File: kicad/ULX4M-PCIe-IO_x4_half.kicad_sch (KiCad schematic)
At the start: 13 parts, among them J10 FCR684205R, J3 SFP+, J4 SFP+, J5 Conn_02x20_Odd_Even, J6 Conn_02x05_Odd_Even, J7 Micro_SD_Card_CD, J8 Conn_02x05_Odd_Even, J9 FCR684205T, P1 HDMI-D, SW1 SW_DIP_x08, SW2 SW_DIP_x08

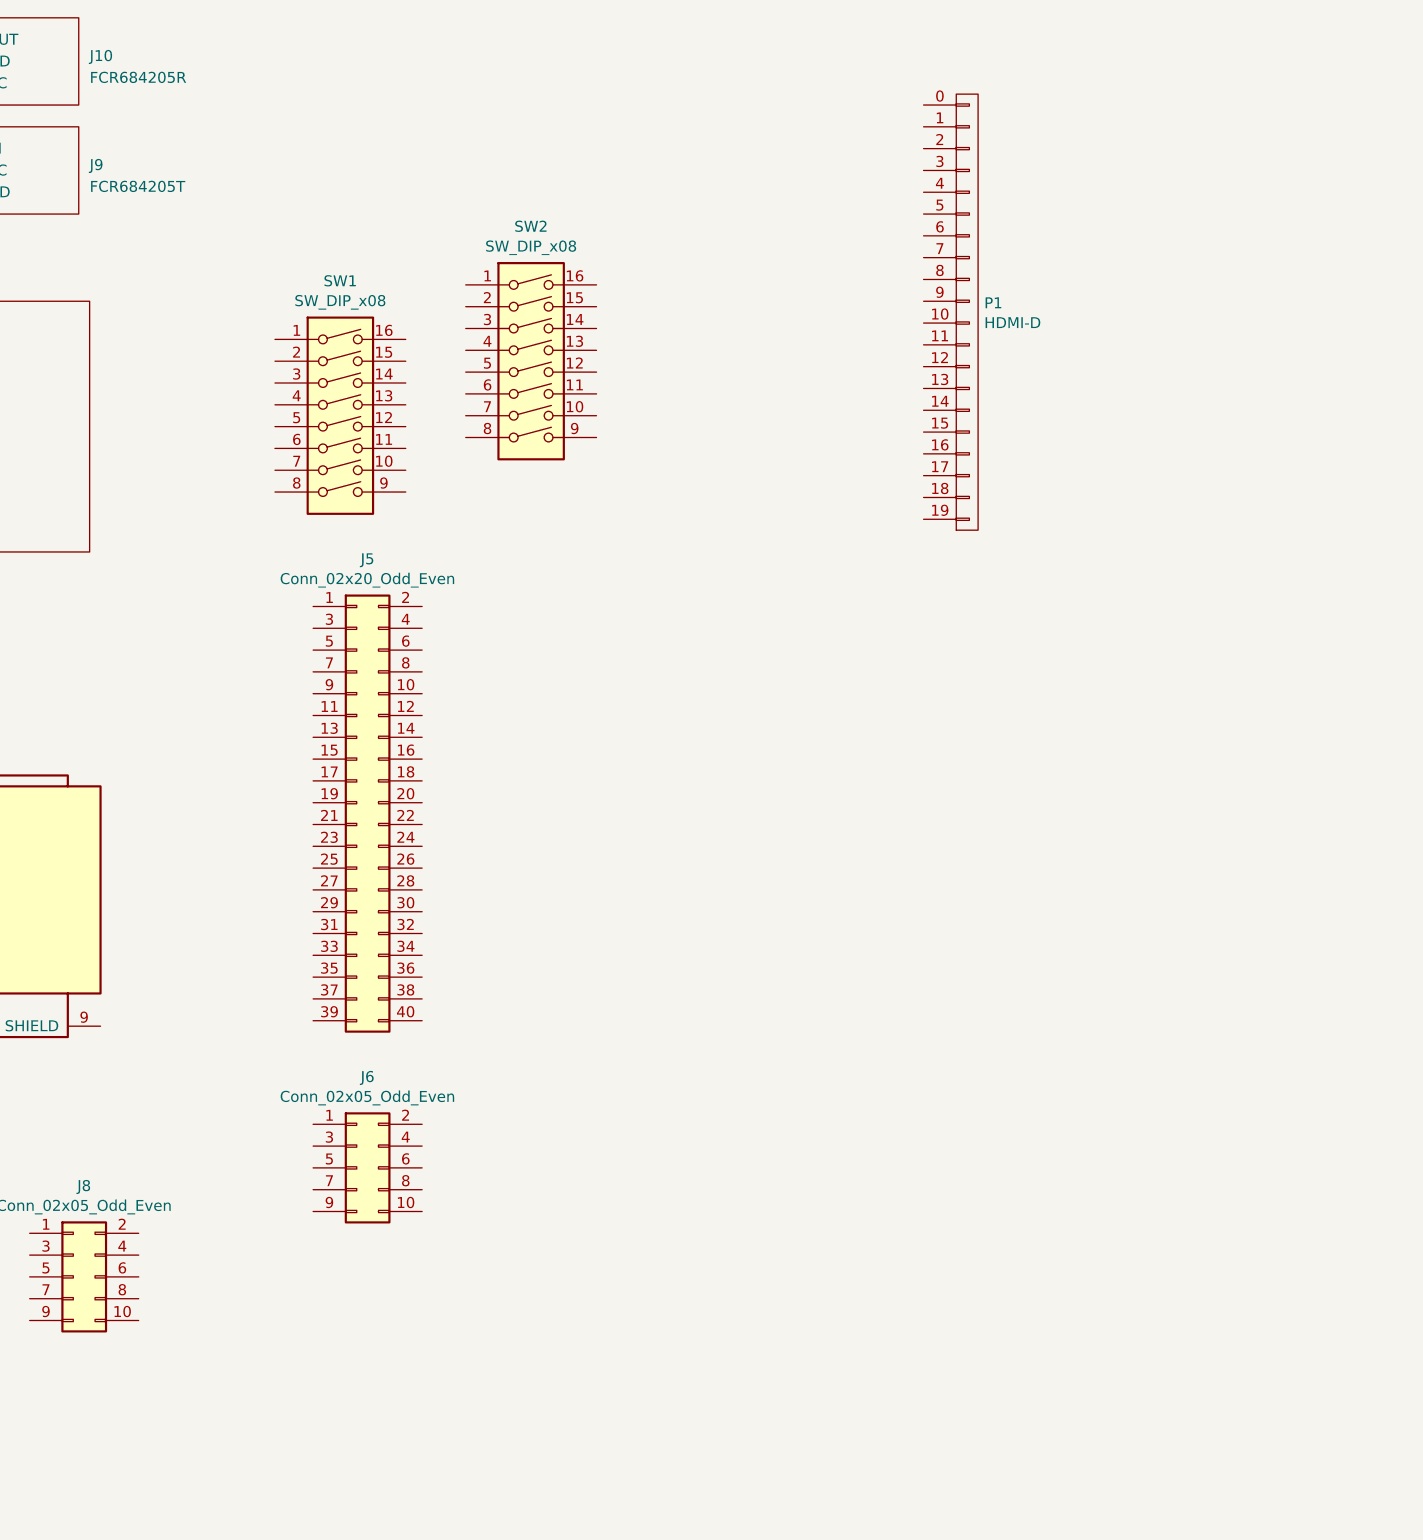
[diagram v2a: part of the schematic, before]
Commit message: Adding PCIe power connector - fix 31
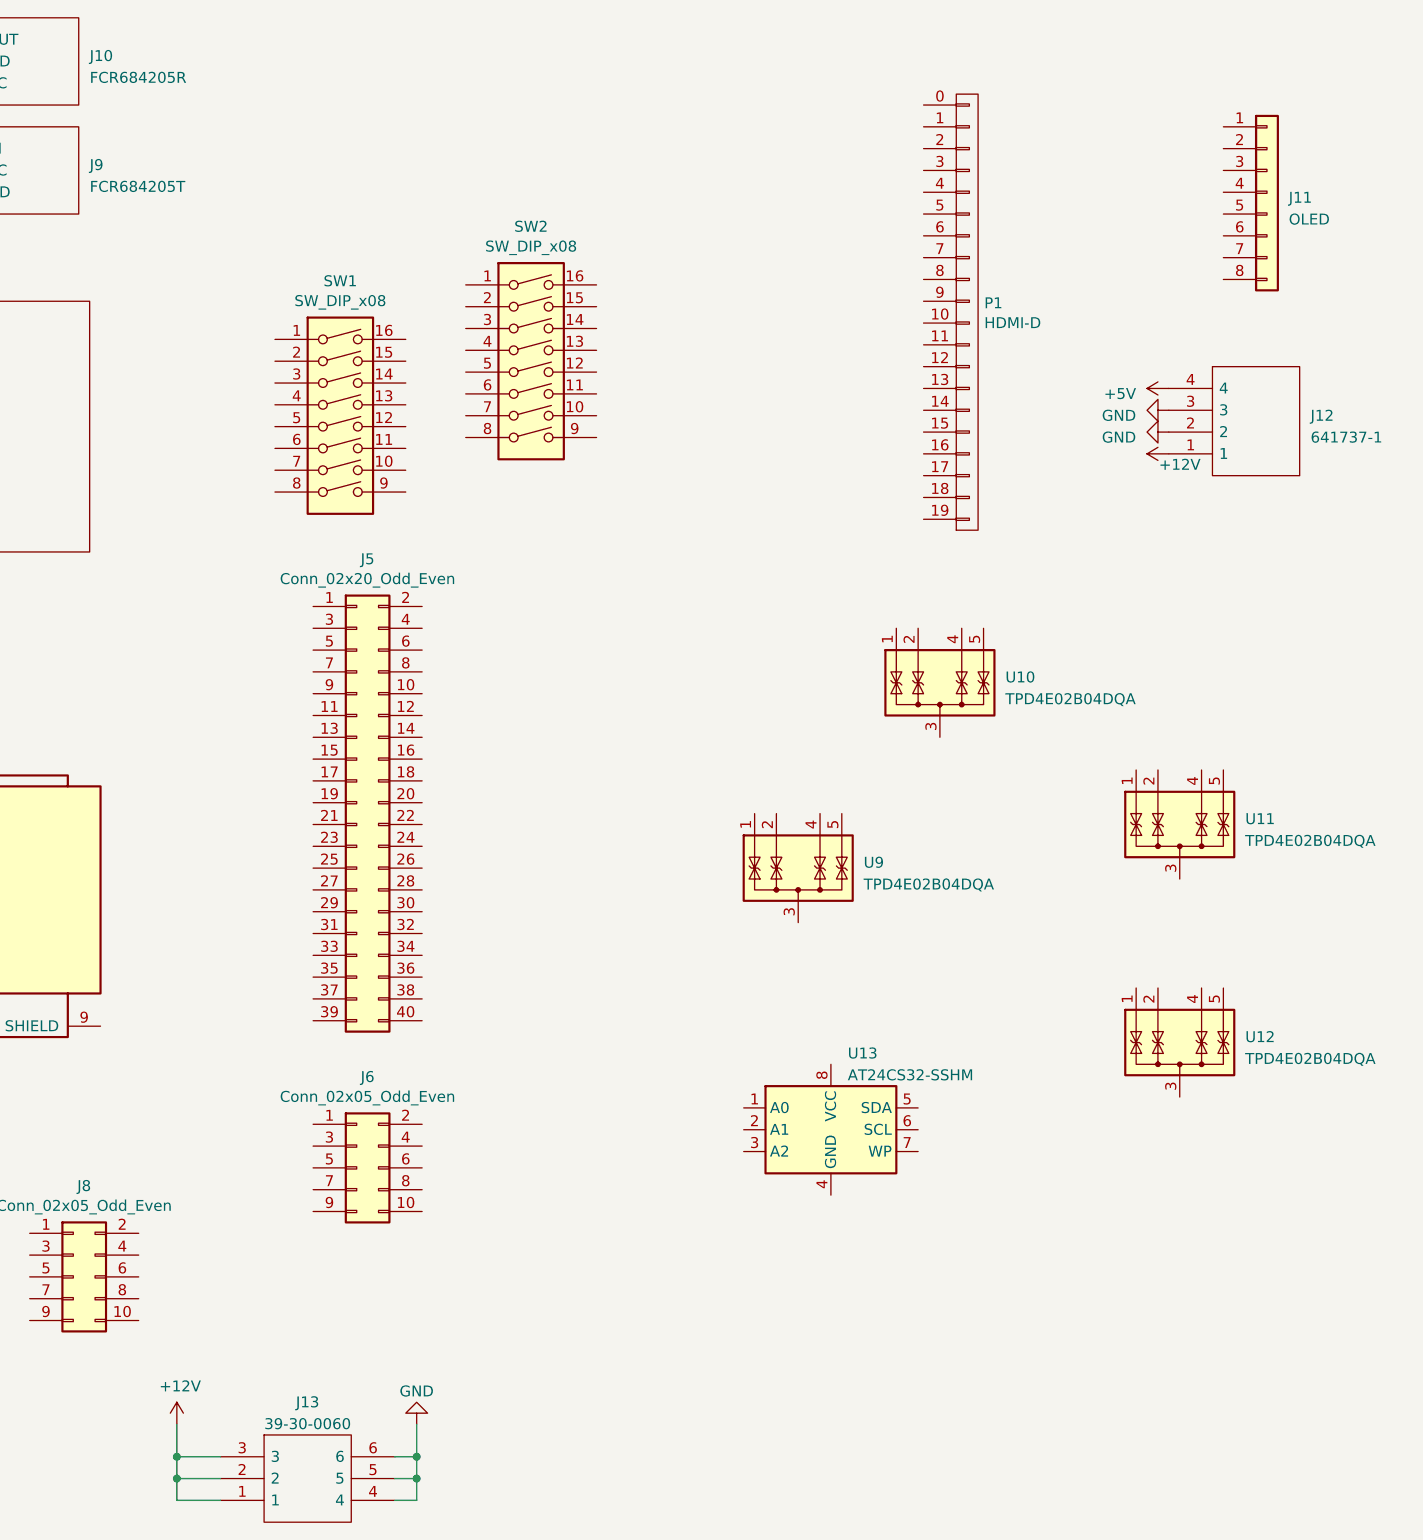
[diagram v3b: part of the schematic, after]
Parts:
- added J11: OLED, Connector_PinHeader_2.54mm:PinHeader_1x08_P2.54mm_Vertical, symbol Connector_Generic:Conn_01x08
- added J12: 641737-1, 641737-1:641737-1, symbol 641737-1:641737-1
- added J13: 39-30-0060, 39-30-0060:39-30-Y060, symbol 39-30-0060:39-30-0060
- added U10, U11, U12, U9: TPD4E02B04DQA, Package_SON:USON-10_2.5x1.0mm_P0.5mm, symbol Power_Protection:TPD4E02B04DQA
- added U13: AT24CS32-SSHM, Package_SO:SOIC-8_3.9x4.9mm_P1.27mm, symbol Memory_EEPROM:AT24CS32-SSHM
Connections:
- new net: U11.3 (G), U11.8 (G)
- new net: U12.3 (G), U12.8 (G)
- new net: U10.3 (G), U10.8 (G)
- new net: U9.3 (G), U9.8 (G)
- new net +12V: J12.1, J13.1, J13.2, J13.3
- new net +5V: J12.4
- new net GND: J12.2, J12.3, J13.4, J13.5, J13.6

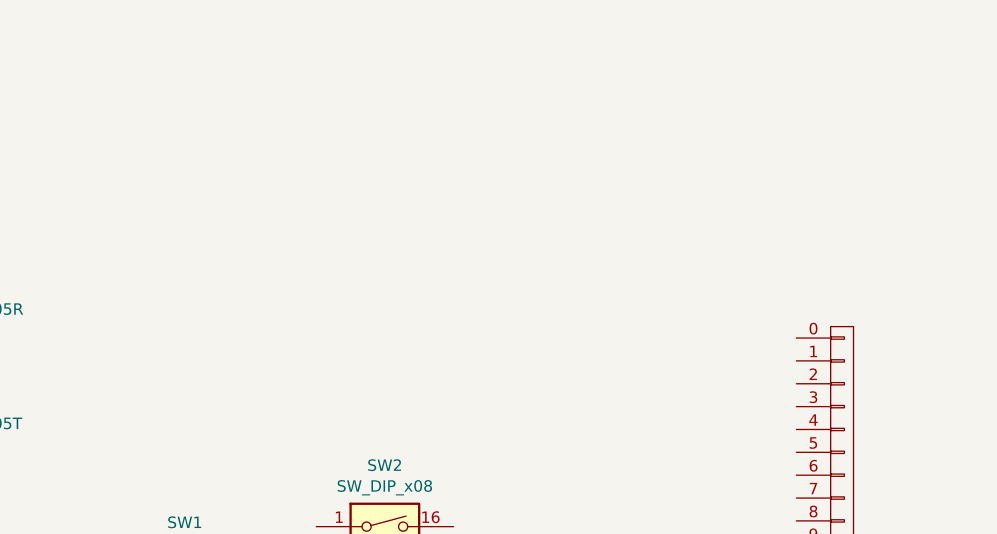
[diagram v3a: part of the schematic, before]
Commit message: Adding LEDs fix #4
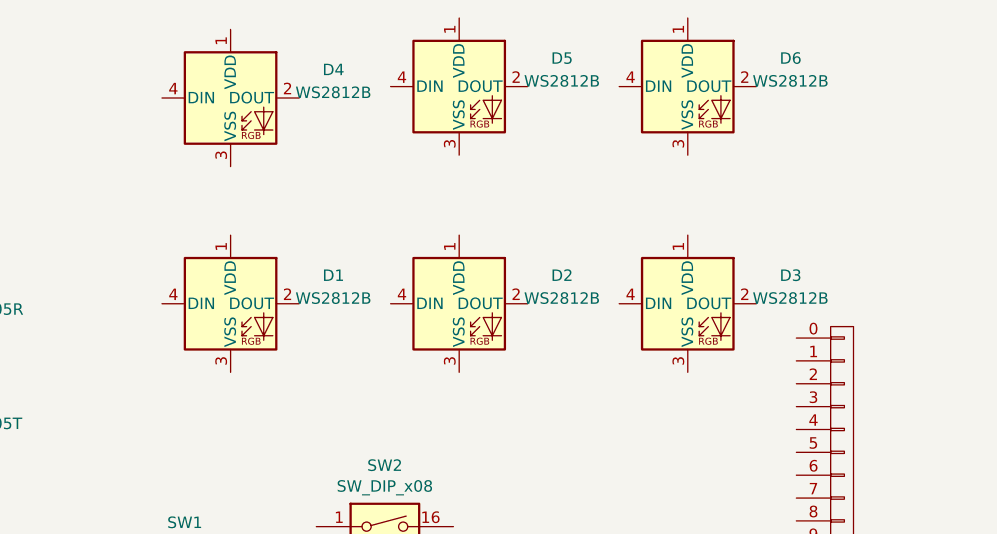
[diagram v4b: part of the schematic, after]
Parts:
- added D1, D2, D3, D4, D5, D6: WS2812B, LED_SMD:LED_WS2812B_PLCC4_5.0x5.0mm_P3.2mm, symbol LED:WS2812B
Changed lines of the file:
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@@
+    )
+  )
+  (symbol (lib_id "LED:WS2812B") (at 189.23 21.59 0) (unit 1)
+    (in_bom yes) (on_board yes) (dnp no) (fields_autoplaced)
+    (property "Reference" "D2" (at 200.66 18.4659 0)
+      (effects (font (size 1.27 1.27)))
+    )
+    (property "Value" "WS2812B" (at 200.66 21.0059 0)
+      (effects (font (size 1.27 1.27)))
+    )
+    (property "Footprint" "LED_SMD:LED_WS2812B_PLCC4_5.0x5.0mm_P3.2mm" (at 190.5 29.21 0)
+      (effects (font (size 1.27 1.27)) (justify left top) hide)
+    )
+    (property "Datasheet" "https://cdn-shop.adafruit.com/datasheets/WS2812B.pdf" (at 191.77 31.115 0)
+      (effects (font (size 1.27 1.27)) (justify left top) hide)
+    )
+    (pin "1")
+    (pin "2")
+    (pin "3")
+    (pin "4")
+    (instances
+      (project "ULX4M-PCIe-IO_x4_half"
+        (path "/e227bafe-08dc-4b2a-9df8-340d24e6faf1"
+          (reference "D2") (unit 1) (value "WS2812B") (footprint "LED_SMD:LED_WS2812B_PLCC4_5.0x5.0mm_P3.2mm")
+        )
+      )
     )
   )
@@
     )
   )
+  (symbol (lib_id "LED:WS2812B") (at 214.63 21.59 0) (unit 1)
+    (in_bom yes) (on_board yes) (dnp no) (fields_autoplaced)
+    (property "Reference" "D3" (at 226.06 18.4659 0)
+      (effects (font (size 1.27 1.27)))
+    )
+    (property "Value" "WS2812B" (at 226.06 21.0059 0)
+      (effects (font (size 1.27 1.27)))
+    )
+    (property "Footprint" "LED_SMD:LED_WS2812B_PLCC4_5.0x5.0mm_P3.2mm" (at 215.9 29.21 0)
+      (effects (font (size 1.27 1.27)) (justify left top) hide)
+    )
+    (property "Datasheet" "https://cdn-shop.adafruit.com/datasheets/WS2812B.pdf" (at 217.17 31.115 0)
+      (effects (font (size 1.27 1.27)) (justify left top) hide)
+    )
+    (pin "1")
+    (pin "2")
+    (pin "3")
+    (pin "4")
+    (instances
+      (project "ULX4M-PCIe-IO_x4_half"
+        (path "/e227bafe-08dc-4b2a-9df8-340d24e6faf1"
+          (reference "D3") (unit 1) (value "WS2812B") (footprint "LED_SMD:LED_WS2812B_PLCC4_5.0x5.0mm_P3.2mm")
+        )
+      )
+    )
+  )
+  (symbol (lib_id "LED:WS2812B") (at 189.23 -2.54 0) (unit 1)
+    (in_bom yes) (on_board yes) (dnp no) (fields_autoplaced)
+    (property "Reference" "D5" (at 200.66 -5.6641 0)
+      (effects (font (size 1.27 1.27)))
+    )
+    (property "Value" "WS2812B" (at 200.66 -3.1241 0)
+      (effects (font (size 1.27 1.27)))
+    )
+    (property "Footprint" "LED_SMD:LED_WS2812B_PLCC4_5.0x5.0mm_P3.2mm" (at 190.5 5.08 0)
+      (effects (font (size 1.27 1.27)) (justify left top) hide)
+    )
+    (property "Datasheet" "https://cdn-shop.adafruit.com/datasheets/WS2812B.pdf" (at 191.77 6.985 0)
+      (effects (font (size 1.27 1.27)) (justify left top) hide)
+    )
+    (pin "1")
+    (pin "2")
+    (pin "3")
+    (pin "4")
+    (instances
+      (project "ULX4M-PCIe-IO_x4_half"
+        (path "/e227bafe-08dc-4b2a-9df8-340d24e6faf1"
+          (reference "D5") (unit 1) (value "WS2812B") (footprint "LED_SMD:LED_WS2812B_PLCC4_5.0x5.0mm_P3.2mm")
+        )
+      )
+    )
+  )
   (symbol (lib_id "power:+12V") (at 139.7 179.07 0) (unit 1)
     (in_bom yes) (on_board yes) (dnp no)
@@
         (path "/e227bafe-08dc-4b2a-9df8-340d24e6faf1"
           (reference "#PWR0120") (unit 1) (value "+5V") (footprint "")
+        )
+      )
+    )
+  )
+  (symbol (lib_id "LED:WS2812B") (at 214.63 -2.54 0) (unit 1)
+    (in_bom yes) (on_board yes) (dnp no) (fields_autoplaced)
+    (property "Reference" "D6" (at 226.06 -5.6641 0)
+      (effects (font (size 1.27 1.27)))
+    )
+    (property "Value" "WS2812B" (at 226.06 -3.1241 0)
+      (effects (font (size 1.27 1.27)))
+    )
+    (property "Footprint" "LED_SMD:LED_WS2812B_PLCC4_5.0x5.0mm_P3.2mm" (at 215.9 5.08 0)
+      (effects (font (size 1.27 1.27)) (justify left top) hide)
+    )
+    (property "Datasheet" "https://cdn-shop.adafruit.com/datasheets/WS2812B.pdf" (at 217.17 6.985 0)
+      (effects (font (size 1.27 1.27)) (justify left top) hide)
+    )
+    (pin "1")
+    (pin "2")
+    (pin "3")
+    (pin "4")
+    (instances
+      (project "ULX4M-PCIe-IO_x4_half"
+        (path "/e227bafe-08dc-4b2a-9df8-340d24e6faf1"
+          (reference "D6") (unit 1) (value "WS2812B") (footprint "LED_SMD:LED_WS2812B_PLCC4_5.0x5.0mm_P3.2mm")
         )
       )
@@
     )
   )
+  (symbol (lib_id "LED:WS2812B") (at 163.83 21.59 0) (unit 1)
+    (in_bom yes) (on_board yes) (dnp no) (fields_autoplaced)
+    (property "Reference" "D1" (at 175.26 18.4659 0)
+      (effects (font (size 1.27 1.27)))
+    )
+    (property "Value" "WS2812B" (at 175.26 21.0059 0)
+      (effects (font (size 1.27 1.27)))
+    )
+    (property "Footprint" "LED_SMD:LED_WS2812B_PLCC4_5.0x5.0mm_P3.2mm" (at 165.1 29.21 0)
+      (effects (font (size 1.27 1.27)) (justify left top) hide)
+    )
+    (property "Datasheet" "https://cdn-shop.adafruit.com/datasheets/WS2812B.pdf" (at 166.37 31.115 0)
+      (effects (font (size 1.27 1.27)) (justify left top) hide)
+    )
+    (pin "1")
+    (pin "2")
+    (pin "3")
+    (pin "4")
+    (instances
+      (project "ULX4M-PCIe-IO_x4_half"
+        (path "/e227bafe-08dc-4b2a-9df8-340d24e6faf1"
+          (reference "D1") (unit 1) (value "WS2812B") (footprint "LED_SMD:LED_WS2812B_PLCC4_5.0x5.0mm_P3.2mm")
+        )
+      )
+    )
+  )
   (symbol (lib_id "power:GND") (at 255.27 63.5 270) (unit 1)
     (in_bom yes) (on_board yes) (dnp no) (fields_autoplaced)
@@
         )
       )
+    )
+  )
+  (symbol (lib_id "LED:WS2812B") (at 163.83 -1.27 0) (unit 1)
+    (in_bom yes) (on_board yes) (dnp no) (fields_autoplaced)
+    (property "Reference" "D4" (at 175.26 -4.3941 0)
+      (effects (font (size 1.27 1.27)))
+    )
+    (property "Value" "WS2812B" (at 175.26 -1.8541 0)
+      (effects (font (size 1.27 1.27)))
+    )
+    (property "Footprint" "LED_SMD:LED_WS2812B_PLCC4_5.0x5.0mm_P3.2mm" (at 165.1 6.35 0)
+      (effects (font (size 1.27 1.27)) (justify left top) hide)
+    )
+    (property "Datasheet" "https://cdn-shop.adafruit.com/datasheets/WS2812B.pdf" (at 166.37 8.255 0)
+      (effects (font (size 1.27 1.27)) (justify left top) hide)
+    )
+    (pin "1")
+    (pin "2")
+    (pin "3")
+    (pin "4")
+    (instances
+      (project "ULX4M-PCIe-IO_x4_half"
+        (path "/e227bafe-08dc-4b2a-9df8-340d24e6faf1"
+          (reference "D4") (unit 1) (value "WS2812B") (footprint "LED_SMD:LED_WS2812B_PLCC4_5.0x5.0mm_P3.2mm")
+        )
+      )

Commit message: Adding more features
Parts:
- added C10: 100nF, Capacitor_SMD:C_0603_1608Metric, symbol Device:C_Small
- added C11: 10nF, Capacitor_SMD:C_0603_1608Metric, symbol Device:C_Small
- added C9: 330nF, Capacitor_SMD:C_0603_1608Metric, symbol Device:C_Small
- added D10: +3.3VA, LED_SMD:LED_0603_1608Metric, symbol Device:LED_Small
- added D7: +12V, LED_SMD:LED_0603_1608Metric, symbol Device:LED_Small
- added D8: +5V, LED_SMD:LED_0603_1608Metric, symbol Device:LED_Small
- added D9: +3.3V, LED_SMD:LED_0603_1608Metric, symbol Device:LED_Small
- added F1: Fuse_5V, Fuse:Fuse_1206_3216Metric, symbol Device:Fuse_Small
- added F2: Fuse_12V, Fuse:Fuse_1206_3216Metric, symbol Device:Fuse_Small
- added H1, H2, H3, H4: HATMountingHole, MountingHole:MountingHole_3.2mm_M3, symbol Mechanical:MountingHole
- added H5, H6, H7, H8: OLEDMountingHole, MountingHole:MountingHole_3.2mm_M3, symbol Mechanical:MountingHole
- added J14: LM7805_EN, Connector_PinHeader_2.54mm:PinHeader_1x02_P2.54mm_Vertical, symbol Connector_Generic:Conn_01x02
- added J15: POE, Connector_PinHeader_2.54mm:PinHeader_2x02_P2.54mm_Vertical, symbol Connector_Generic:Conn_02x02_Odd_Even
- added R10: R220, Resistor_SMD:R_0603_1608Metric, symbol Device:R_Small
- added R11, R12: R120, Resistor_SMD:R_0603_1608Metric, symbol Device:R_Small
- added R9: R510, Resistor_SMD:R_0603_1608Metric, symbol Device:R_Small
- added U14: LM78M05_TO252, Package_TO_SOT_SMD:TO-252-2, symbol Regulator_Linear:LM78M05_TO252
- AE1: value Antenna_Dipole -> EXT_CLK_REF1; footprint Connector_Coaxial:SMA_Amphenol_132289_EdgeMount -> Connector_Coaxial:SMA_Amphenol_132291-12_Vertical
- AE2: value Antenna_Dipole -> EXT_CLK_REF2; footprint Connector_Coaxial:SMA_Amphenol_132289_EdgeMount -> Connector_Coaxial:SMA_Amphenol_132291-12_Vertical
- J5: value Conn_02x20_Odd_Even -> HAT; footprint Connector_PinHeader_2.54mm:PinHeader_2x20_P2.54mm_Vertical_SMD -> Connector_PinHeader_2.54mm:PinHeader_2x20_P2.54mm_Vertical
- J6: value Conn_02x05_Odd_Even -> EXT_USB; footprint Connector_PinHeader_2.54mm:PinHeader_2x05_P2.54mm_Vertical_SMD -> Connector_PinHeader_2.54mm:PinHeader_2x05_P2.54mm_Vertical
- J7: footprint micro-sd:SCHD3A100 -> Connector_Card:microSD_HC_Molex_104031-0811
- J8: value Conn_02x05_Odd_Even -> Board_To_Board
- P1: footprint hdmi-d:HDMI-D -> conn-fci:CONN-10029449-111RLF
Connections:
- net +12V: now also C9.1, F2.1, R9.1, U14.1 (VI); no longer J12.1
- net +5V: now also F1.1, J14.1 (Pin_1), R10.1; no longer J12.4
- net GND: now also C10.2, C11.2, C9.2, D10.1 (K), D7.1 (K), D8.1 (K), D9.1 (K), U14.2 (GND)
- new net: D10.2 (A), R12.2
- new net: D7.2 (A), R9.2
- new net: D8.2 (A), R10.2
- new net: C10.1, C11.1, J14.2 (Pin_2), U14.3 (VO)
- new net: F2.2, J12.1
- new net: F1.2, J12.4
- new net: D9.2 (A), R11.2
- new net +3.3V: R11.1
- new net +3.3VA: R12.1
